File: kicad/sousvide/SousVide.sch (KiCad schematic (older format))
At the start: 18 parts, among them P1 Rotary Encoder, P2 Relay 5v, P3 DS18B20, P4 FTDI, P5 OLED 1306, P6 USB_A, Q1 PN2222A, U1 AP1117, U2 ESP-12

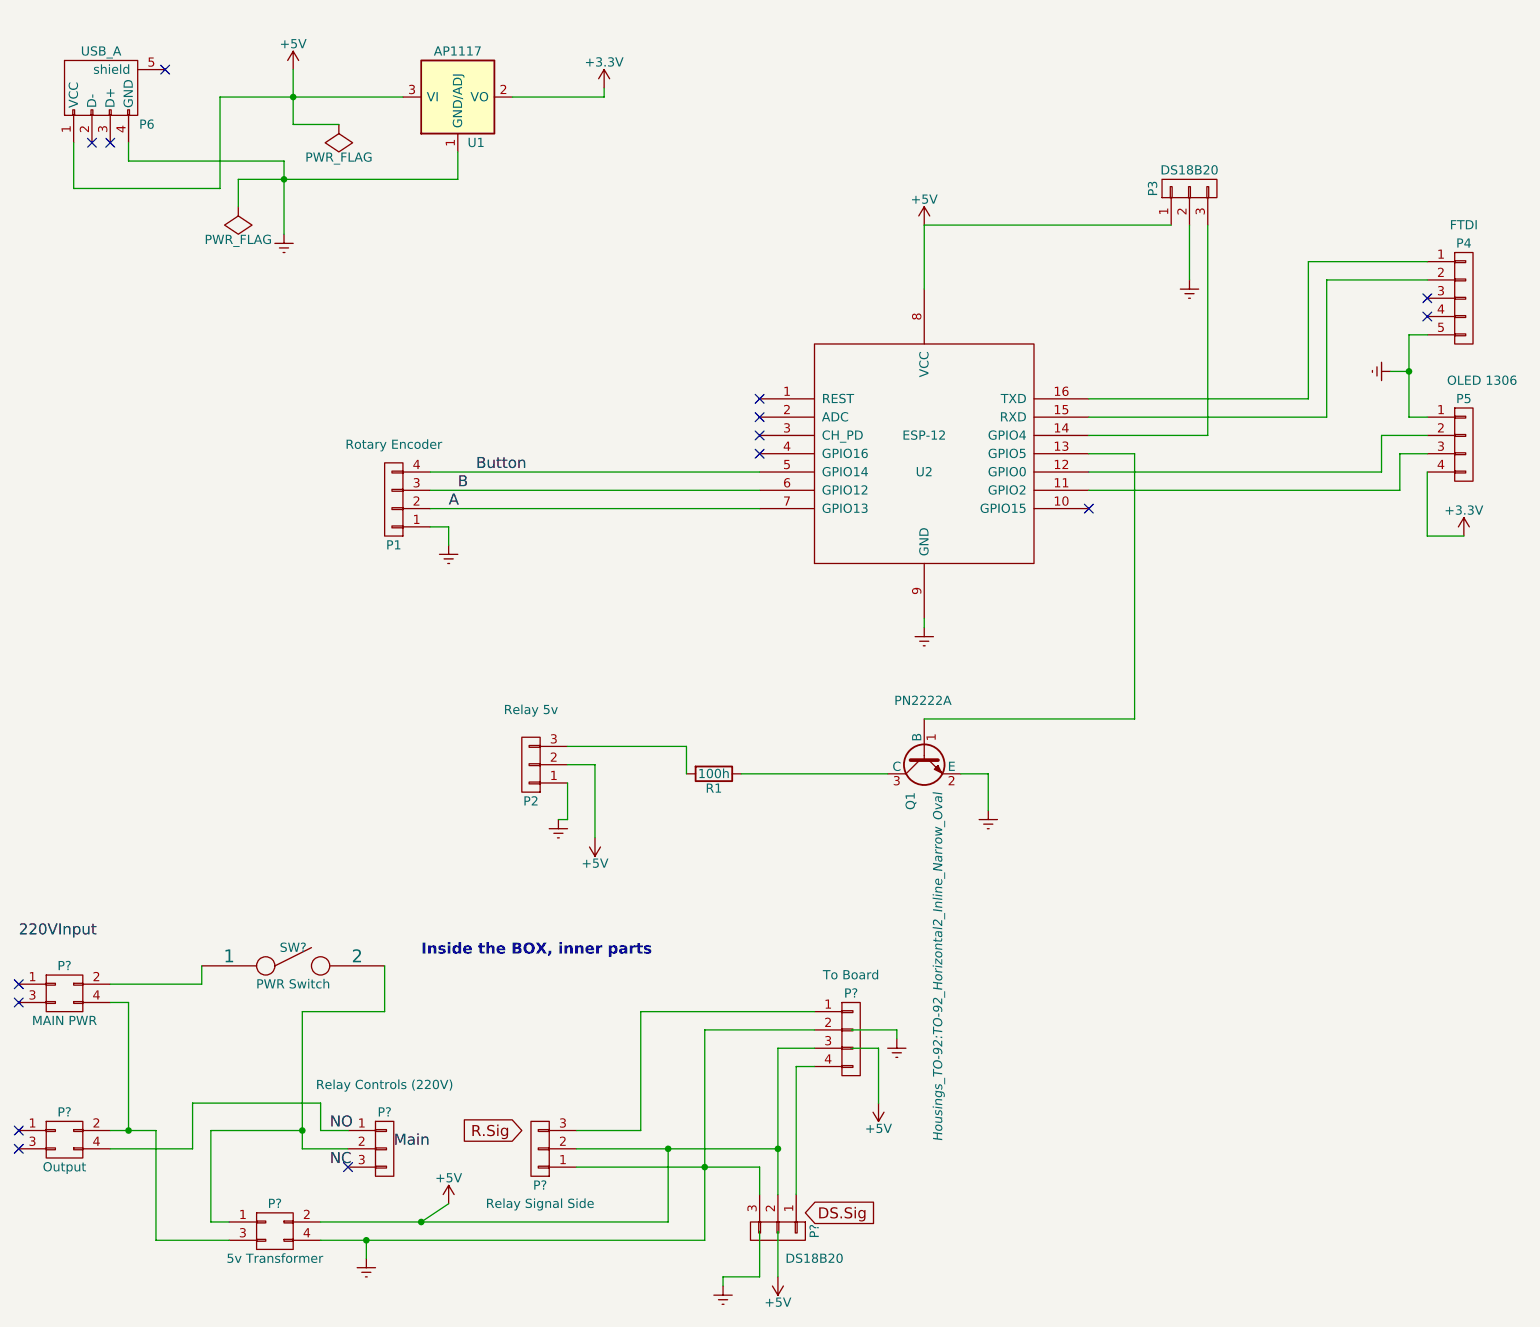
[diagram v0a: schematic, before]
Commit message: New schematic and pin assignments
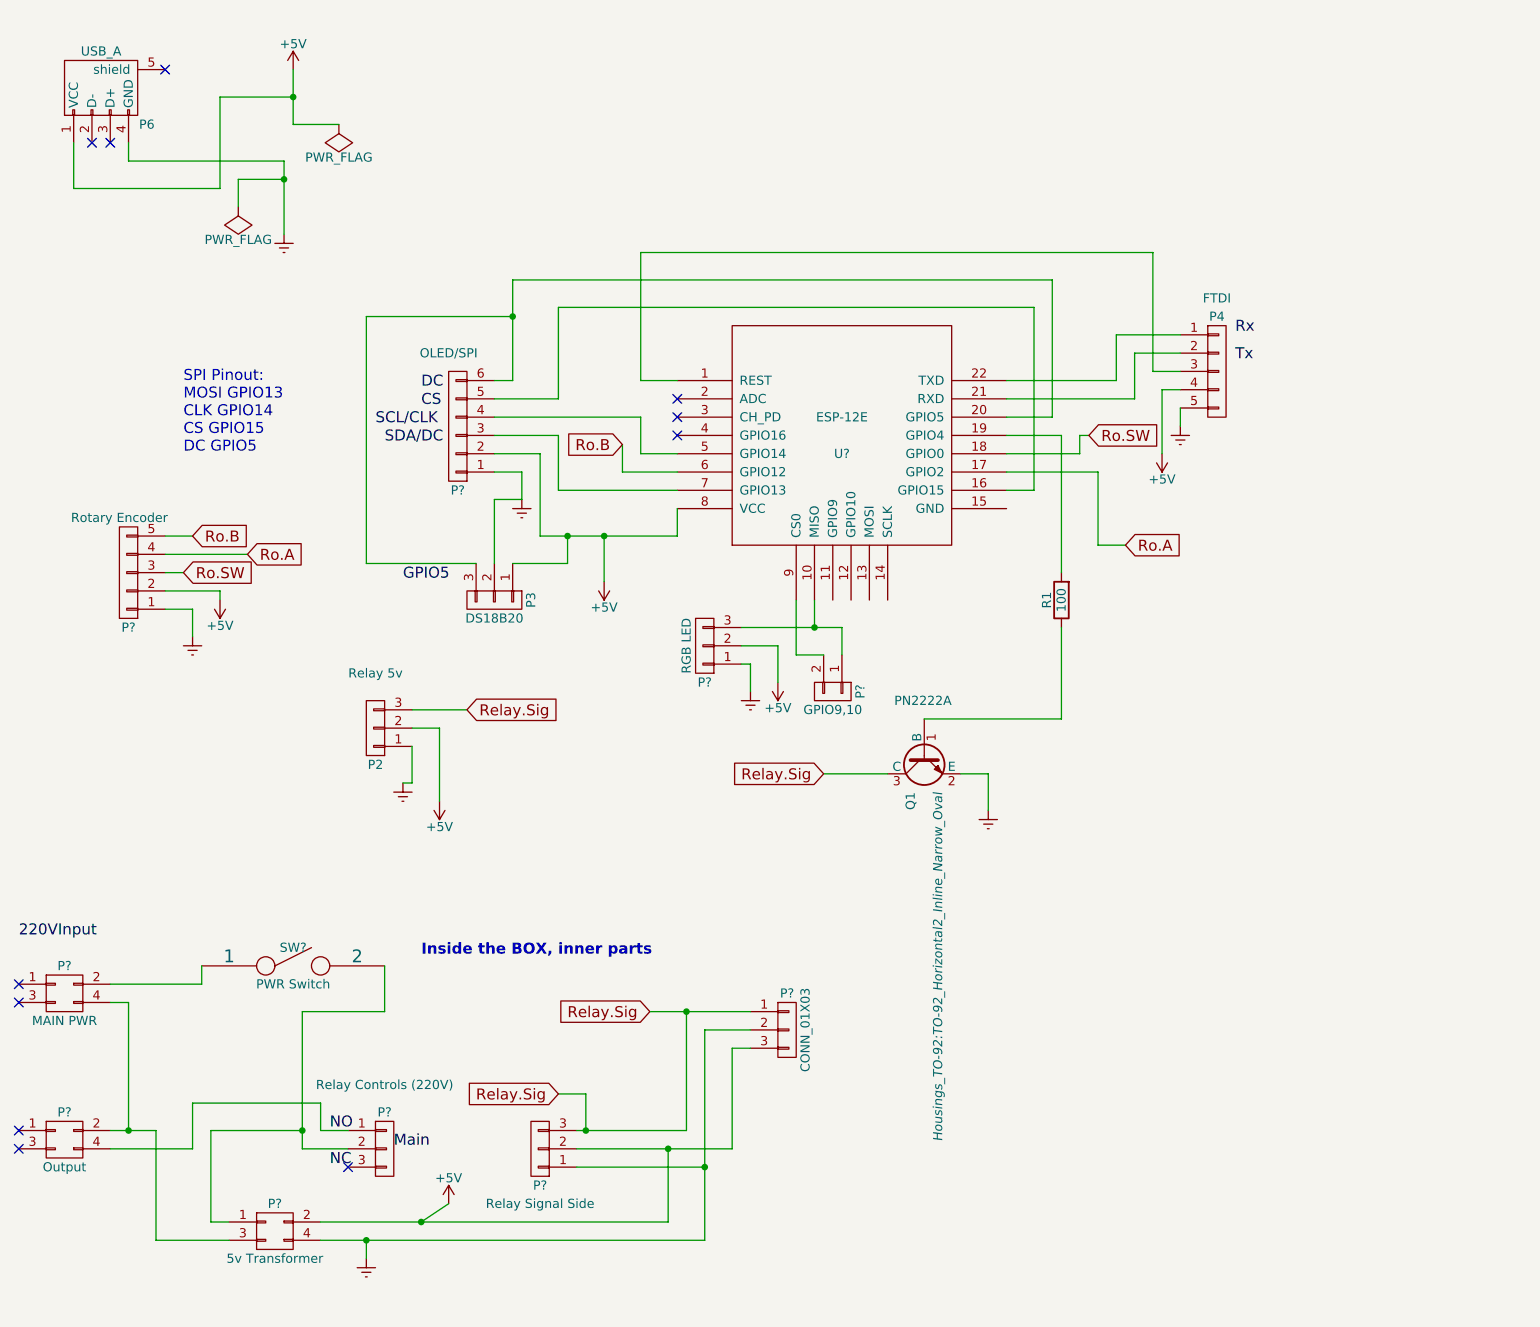
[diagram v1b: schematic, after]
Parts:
- removed P1: Rotary Encoder, Pin_Headers:Pin_Header_Angled_1x04, symbol CONN_01X04
- removed P5: OLED 1306, Pin_Headers:Pin_Header_Angled_1x04, symbol CONN_01X04
- removed P?: To Board, symbol CONN_01X04
- removed P?: DS18B20, symbol CONN_01X03
- removed U1: AP1117, Buttons_Switches_ThroughHole:SW_DIP_x1_Slide, symbol AP1117
- removed U2: ESP-12, Buttons_Switches_ThroughHole:SW_DIP_x7_Piano, symbol ESP-12
- added P?: CONN_01X03, symbol CONN_01X03
- added P?: RGB LED, symbol CONN_01X03
- added P?: Rotary Encoder, symbol CONN_01X05
- added P?: OLED/SPI, symbol CONN_01X06
- added P?: GPIO9,10, symbol CONN_01X02
- added U?: ESP-12E, symbol ESP-12E
- R1: value 100h -> 100
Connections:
- net labels added: CS, DC, GPIO5, Relay.Sig, Ro.A, Ro.B, Ro.SW, Rx, SCL/CLK, SDA/DC, Tx
- net labels removed: +3.3V, A, B, Button, DS.Sig, R.Sig
- wire segments 99 -> 126
- no-connect marks 15 -> 11
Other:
- note added: "SPI Pinout: \nMOSI GPIO13 \nCLK GPIO14\nCS GPIO15 \nDC GPIO5"
- moved on the sheet: P2, P3, P4, R1

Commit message: simplification with extra data, move goose around,and simplify settings
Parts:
- removed Q1: PN2222A, Housings_TO-92:TO-92_Horizontal2_Inline_Narrow_Oval, symbol PN2222A
- added C?: CP, symbol CP
- added U?: AP1117, symbol AP1117
- R1: value 100 -> 330
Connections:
- net +5V: now also C?.1, U?.3 (VI); no longer P?.2 (P2)
- net Earth: now also C?.2, U?.1 (GND/ADJ)
- net Relay.Sig: now also R1.1
- new net +3V3: P?.2 (P2), U?.2 (VO)
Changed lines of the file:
@@
-$EndComp
-$Comp
-L PN2222A Q1
-U 1 1 55E5857F
-P 5650 4700
-F 0 "Q1" H 5850 4775 50  0000 L CNN
-F 1 "PN2222A" V 5350 4550 50  0000 L CNN
-F 2 "Housings_TO-92:TO-92_Horizontal2_Inline_Narrow_Oval" H 5850 4625 50  0000 L CIN
-F 3 "" H 5650 4700 50  0000 L CNN
-	1    5650 4700
-	0    -1   1    0
 $EndComp
 $Comp
@@
 P 6400 3850
 F 0 "R1" V 6480 3850 50  0000 C CNN
-F 1 "100" V 6400 3850 50  0000 C CNN
+F 1 "330" V 6400 3850 50  0000 C CNN
 F 2 "Resistors_ThroughHole:Resistor_Horizontal_RM10mm" V 6330 3850 30  0001 C CNN
 F 3 "" H 6400 3850 30  0000 C CNN
@@
 	1    3000 4950
 	-1   0    0    1
-$EndComp
-$Comp
-L Earth #PWR08
-U 1 1 55E59D42
-P 6000 5000
-F 0 "#PWR08" H 6000 4750 50  0001 C CNN
-F 1 "Earth" H 6000 4850 50  0001 C CNN
-F 2 "" H 6000 5000 60  0000 C CNN
-F 3 "" H 6000 5000 60  0000 C CNN
-	1    6000 5000
-	1    0    0    -1
 $EndComp
 $Comp
@@
 NoConn ~ 4300 2950
 $Comp
-L +5V #PWR?
-U 1 1 562819E3
-P 1800 3850
-F 0 "#PWR?" H 1800 3700 50  0001 C CNN
-F 1 "+5V" H 1800 3990 50  0000 C CNN
-F 2 "" H 1800 3850 60  0000 C CNN
-F 3 "" H 1800 3850 60  0000 C CNN
-	1    1800 3850
-	-1   0    0    1
-$EndComp
-$Comp
 L Earth #PWR?
 U 1 1 562895E9
@@
 	2850 4850 2800 4850
 Wire Wire Line
-	6400 4500 5650 4500
-Wire Wire Line
 	2850 4550 3000 4550
 Wire Wire Line
 	3000 4550 3000 4950
-Wire Wire Line
-	5850 4800 6000 4800
-Wire Wire Line
-	6000 4800 6000 5000
 Wire Wire Line
 	1500 3900 1650 3900
@@
 Connection ~ 2200 1100
 Wire Wire Line
-	1300 1450 2150 1450
-Wire Wire Line
 	1300 1450 1300 1350
 Wire Wire Line
 	2150 1450 2150 1850
 Wire Wire Line
-	1000 1350 1000 1600
+	1000 1350 1000 1850
 Wire Wire Line
 	1000 1600 1800 1600
@@
 	1800 1600 1800 1100
 Wire Wire Line
-	2200 1250 2450 1250
-Wire Wire Line
-	1900 1550 2150 1550
+	2200 1250 2700 1250
+Wire Wire Line
+	1900 1550 3000 1550
 Wire Wire Line
 	1900 1700 1900 1550
@@
 Wire Wire Line
 	4650 4000 5200 4000
-Wire Wire Line
-	1500 3800 1800 3800
-Wire Wire Line
-	1800 3800 1800 3850
 Wire Wire Line
 	3450 3300 3450 3150
@@
 Text GLabel 3650 6550 0    60   Input ~ 0
 Relay.Sig
-Text GLabel 5100 4800 0    60   Input ~ 0
+Text GLabel 6400 4150 0    60   Input ~ 0
 Relay.Sig
 Connection ~ 4350 6100
@@
 Ro.B
 Wire Wire Line
-	5100 4800 5450 4800
-Wire Wire Line
-	6400 4500 6400 4000
+	6400 4000 6400 4150
 Wire Wire Line
 	6400 2950 6400 3700
@@
 	5200 4000 5200 4150
 Connection ~ 5050 4000
+$Comp
+L AP1117 U?
+U 1 1 562B5B86
+P 3000 950
+F 0 "U?" H 3100 700 50  0000 C CNN
+F 1 "AP1117" H 3000 1200 50  0000 C CNN
+F 2 "" H 3000 950 60  0000 C CNN
+F 3 "" H 3000 950 60  0000 C CNN
+	1    3000 950
+	1    0    0    -1
+$EndComp
+Wire Wire Line
+	2700 1250 2700 950
+Connection ~ 2450 1250
+Wire Wire Line
+	3000 1550 3000 1250
+$Comp
+L CP C?
+U 1 1 562B673B
+P 1250 1850
+F 0 "C?" H 1275 1950 50  0000 L CNN
+F 1 "CP" H 1275 1750 50  0000 L CNN
+F 2 "" H 1288 1700 30  0000 C CNN
+F 3 "" H 1250 1850 60  0000 C CNN
+	1    1250 1850
+	0    -1   -1   0
+$EndComp
+Connection ~ 1000 1600
+Wire Wire Line
+	1300 1450 2150 1450
+Wire Wire Line
+	1000 1850 1100 1850
+Connection ~ 1500 1450
+Wire Wire Line
+	1400 1850 1500 1850
+Wire Wire Line
+	1500 1850 1500 1450
+$Comp
+L +3.3V #PWR?
+U 1 1 562B781B
+P 3450 850
+F 0 "#PWR?" H 3450 700 50  0001 C CNN
+F 1 "+3.3V" H 3450 990 50  0000 C CNN
+F 2 "" H 3450 850 60  0000 C CNN
+F 3 "" H 3450 850 60  0000 C CNN
+	1    3450 850
+	1    0    0    -1
+$EndComp
+Wire Wire Line
+	3300 950  3450 950
+Wire Wire Line
+	3450 950  3450 850
+$Comp
+L +3.3V #PWR?
+U 1 1 562B791B
+P 1850 4000
+F 0 "#PWR?" H 1850 3850 50  0001 C CNN
+F 1 "+3.3V" H 1850 4140 50  0000 C CNN
+F 2 "" H 1850 4000 60  0000 C CNN
+F 3 "" H 1850 4000 60  0000 C CNN
+	1    1850 4000
+	1    0    0    -1
+$EndComp
+Wire Wire Line
+	1500 3800 1700 3800
+Wire Wire Line
+	1700 3800 1700 4000
+Wire Wire Line
+	1700 4000 1850 4000
 $EndSCHEMATC

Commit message: Fixed read
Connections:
- net at R1.2: now also U?.17 (GPIO2); no longer U?.19 (GPIO4)
- net at P?.6 (P6), U?.20 (GPIO5): no longer P3.3 (P3)
- net Ro.A renamed Ro.DT
- net Ro.DT: now also U?.6 (GPIO12); no longer U?.17 (GPIO2)
- net Ro.B renamed Ro.CLK
- net Ro.CLK: now also U?.19 (GPIO4); no longer U?.6 (GPIO12)
